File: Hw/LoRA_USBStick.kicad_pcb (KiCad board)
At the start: 2 copper layers, 65 x 18 mm, 16 parts, among them J10 USB_B, J4 SWD, SW1 RST, U1 ATSAMD21E, U2 RFM95W-868S2, U7 AP2114H-3.3TRG1

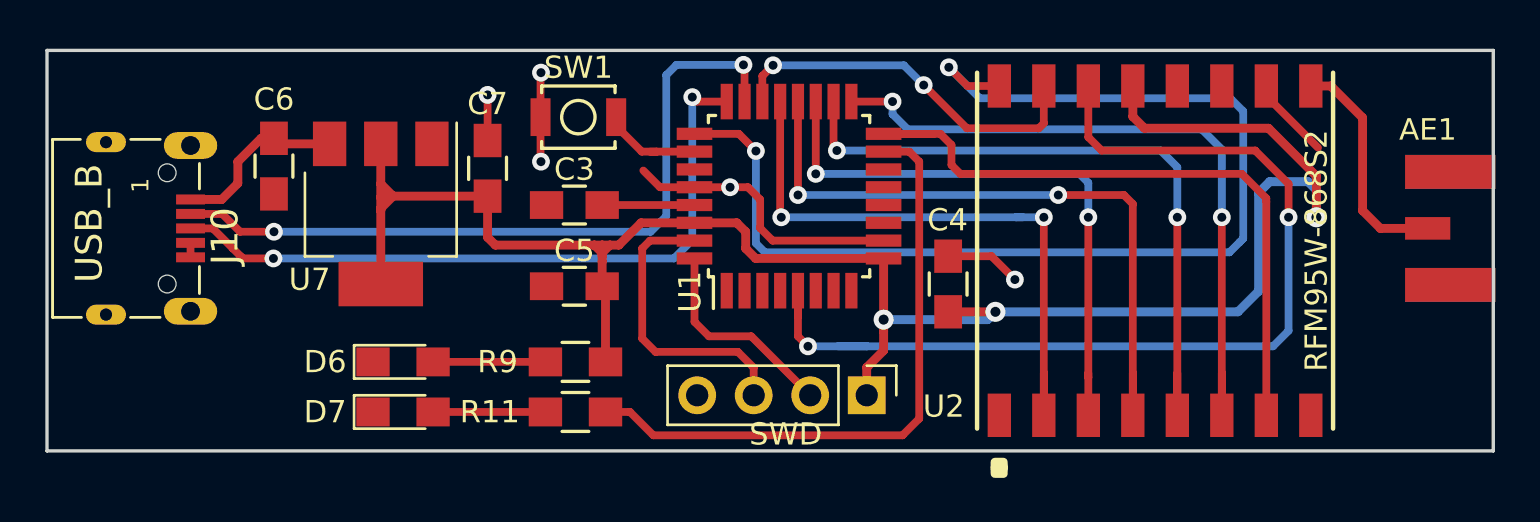
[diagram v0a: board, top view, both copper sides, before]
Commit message: Update kicad 5
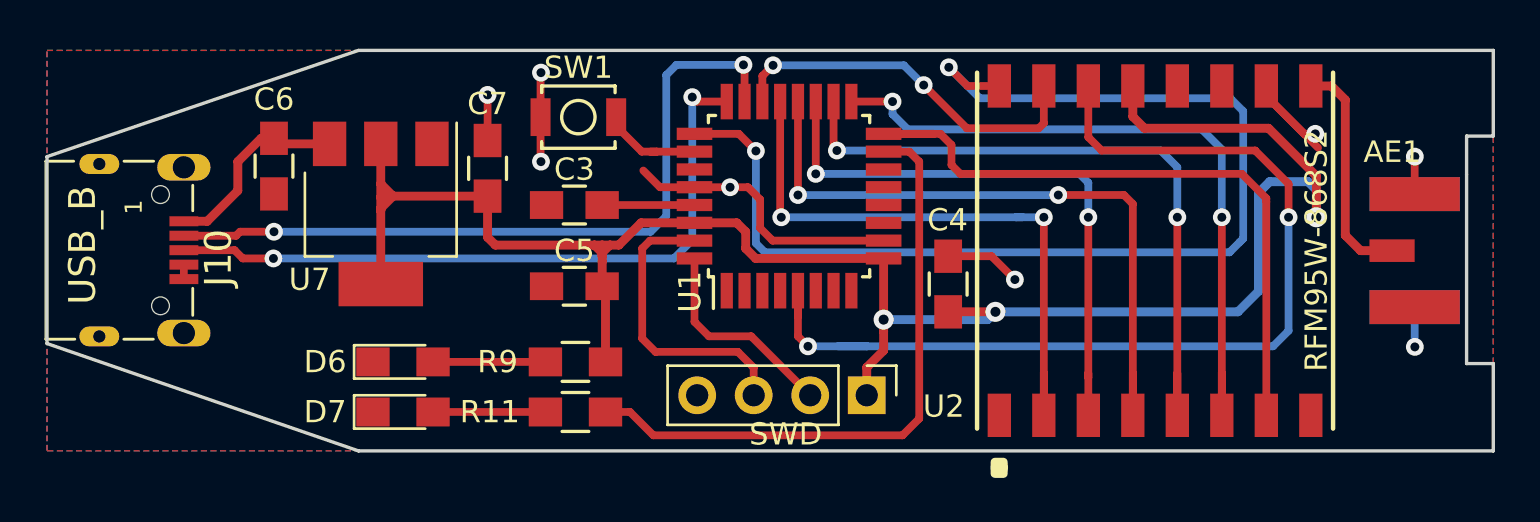
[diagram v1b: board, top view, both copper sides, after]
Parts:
- added G***: LOGO, Aesthetics:electronic_cats_logo_8x6, B.Cu at (196.8, 102.8)
- moved AE1 1.89 mm to (215.5, 104.0)
- moved J10 1.02 mm to (157.1, 104.0)
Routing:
- net GND: track 26.7 -> 33.1 mm, vias 5 -> 8
- net VBUS: track 8.06 -> 8.96 mm
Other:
- outline, holes or cut-outs redrawn
- board text added: "3.3v"
- board text added: "Compatible with LoRaWAN®"
- board text added: "GND"
- board text added: "Notas:"
- board text added: "SWCLK"
- board text added: "SWDIO"
- board text added: "USB-Stick V1.0 CatWAN"

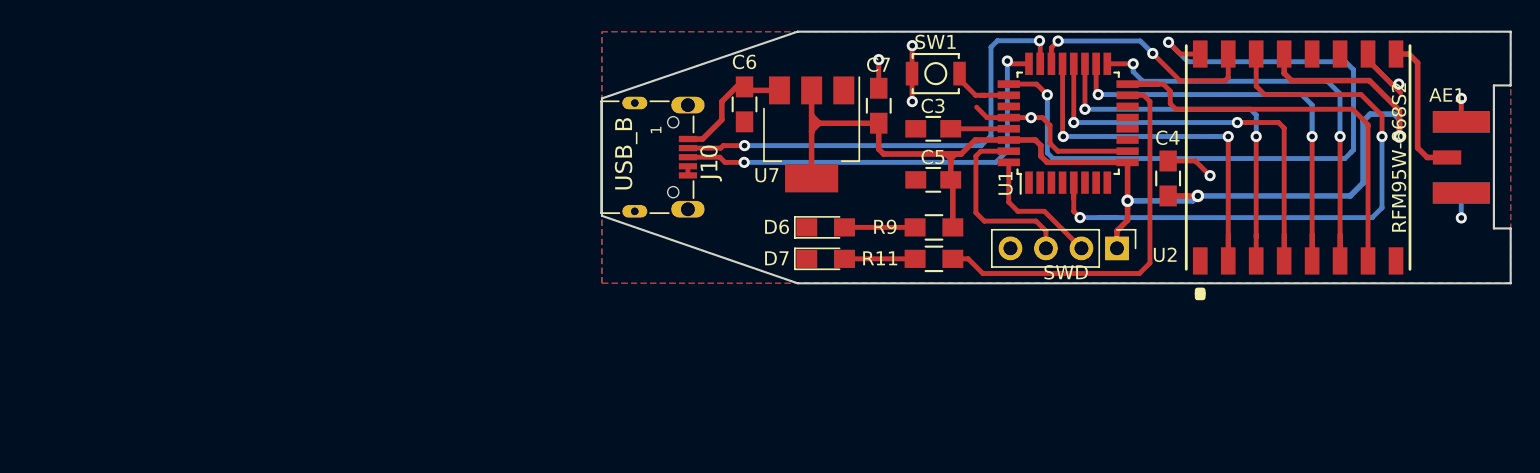
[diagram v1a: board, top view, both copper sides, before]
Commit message: Update measure for case
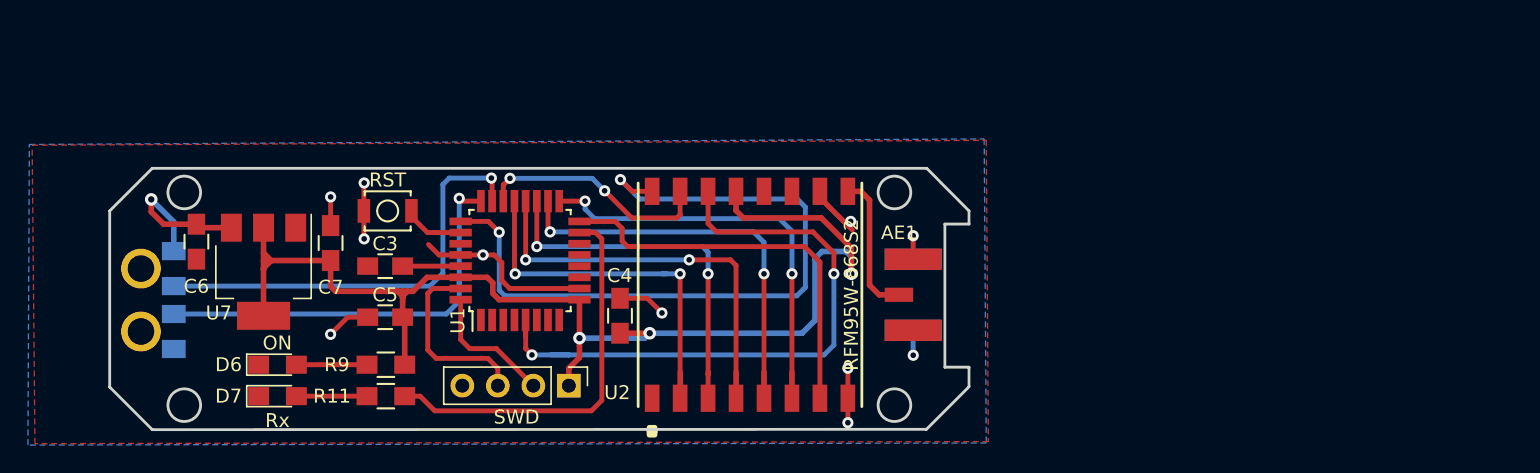
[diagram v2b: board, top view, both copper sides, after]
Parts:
- J10: footprint USB:629105150521 -> USB:629004113921; moved to B.Cu
- moved AE1 40.4 mm to (176.3, 113.8)
- moved C3 40.4 mm to (136.5, 111.8)
- moved C4 40.4 mm to (153.3, 115.3)
- moved C5 40.4 mm to (136.5, 115.4)
- moved C7 40.4 mm to (132.6, 110.1)
- moved D6 40.4 mm to (128.8, 118.8)
- moved D7 40.4 mm to (128.8, 121.1)
- moved J4 40.4 mm to (149.6, 120.3)
- moved R11 40.4 mm to (136.5, 121.1)
- moved R9 40.4 mm to (136.5, 118.8)
- moved SW1 40.4 mm to (136.7, 107.8)
- moved U1 40.4 mm to (146.1, 111.4)
- moved U2 40.4 mm to (162.6, 113.8)
- moved U7 40.4 mm to (127.8, 112.2)
- moved C6 40.4 mm to (123.0, 110.0)
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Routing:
- net GND: track 33.1 -> 39.5 mm, vias 8 -> 11
- net VBUS: track 8.96 -> 11.5 mm, vias 0 -> 1
- net /D-: track 33.7 -> 31.3 mm, vias 2 -> 1
- net /D+: track 31.4 -> 30.5 mm, vias 2 -> 1
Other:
- board size 65 x 18 mm -> 61.5 x 18.7 mm
- board text added: "ON"

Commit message: Fix notes text
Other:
- board text added: "Notes:"
- board text removed: "Notas:"
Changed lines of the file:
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@@
     (visible_elements FFFFFF7F)
     (pcbplotparams
-      (layerselection 0x010fc_80000001)
-      (usegerberextensions false)
+      (layerselection 0x010fc_ffffffff)
+      (usegerberextensions true)
       (usegerberattributes false)
       (usegerberadvancedattributes false)
@@
       (drillshape 0)
       (scaleselection 1)
-      (outputdirectory "/Volumes/Macintosh_HD/Documents/Electronic_Cats/Proyectos/Hw/agroin/Hw/Gerbers/"))
+      (outputdirectory "USB_stick_gerber/"))
   )
   (net 0 "")
@@
     (effects (font (size 1.5 1.5) (thickness 0.3)) (justify mirror))
   )
-  (gr_text Notas: (at 137.292 106.0724) (layer B.SilkS)
+  (gr_text Notes: (at 137.292 106.0724) (layer B.SilkS)
     (effects (font (size 1.5 1.5) (thickness 0.3)) (justify mirror))
   )

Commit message: Change USB side version 1.1v
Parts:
- C6, C7, U7: moved to B.Cu
- J10: moved to F.Cu
- moved C6 4.23 mm to (123.1, 114.2), turned to 90 degrees
- moved C7 4.13 mm to (132.5, 114.2), turned to 270 degrees
- moved SW1 2.58 mm to (136.7, 110.4)
- moved C3 1.44 mm to (136.7, 113.2)
- moved C5 0.16 mm to (136.7, 115.4)
- turned J10 to 270 degrees
- turned U7 to 90 degrees
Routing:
- net VBUS: track 11.5 -> 6.72 mm
- net +3V3: track 87.7 -> 92.1 mm, vias 3 -> 4
- net GND: track 39.5 -> 37.2 mm, vias 11 -> 12
- net /D+: track 30.5 -> 28.2 mm, vias 1 -> 0
- net /SWCLK: track 13.3 -> 11.6 mm
- net /D-: track 31.3 -> 31.9 mm, vias 1 -> 2
- net /RST: track 4.70 -> 4.18 mm
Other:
- board text added: "USB-Stick V1.1 CatWAN"
- board text removed: "USB-Stick V1.0 CatWAN"

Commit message: Fix vias on PCB
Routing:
- net GND: track 37.2 -> 41.1 mm, vias 12 -> 14
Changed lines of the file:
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@@
     (thickness 1.6)
     (drawings 37)
-    (tracks 255)
+    (tracks 261)
     (zones 0)
     (modules 17)
@@
   )
   (layers
-    (0 F.Cu signal hide)
-    (31 B.Cu signal hide)
+    (0 F.Cu signal)
+    (31 B.Cu signal)
     (32 B.Adhes user)
     (33 F.Adhes user)
@@
   (via (at 133.9 113.2) (size 0.8) (drill 0.4) (layers F.Cu B.Cu) (net 1))
   (segment (start 135.4 113.2) (end 133.9 113.2) (width 0.35) (layer F.Cu) (net 1))
+  (via (at 121.4 108.9) (size 0.8) (drill 0.4) (layers F.Cu B.Cu) (net 1))
+  (segment (start 121.3744 108.9256) (end 121.4 108.9) (width 0.35) (layer F.Cu) (net 1))
+  (segment (start 121.3744 110.6984) (end 121.3744 108.9256) (width 0.35) (layer F.Cu) (net 1))
+  (via (at 123.45 110.7) (size 0.8) (drill 0.4) (layers F.Cu B.Cu) (net 1))
+  (segment (start 123.4484 110.6984) (end 123.45 110.7) (width 0.35) (layer F.Cu) (net 1))
+  (segment (start 121.3744 110.6984) (end 123.4484 110.6984) (width 0.35) (layer F.Cu) (net 1))
   (segment (start 170.517 106.4224) (end 169.592 106.4224) (width 0.4) (layer F.Cu) (net 2))
   (segment (start 171.142 107.0474) (end 170.517 106.4224) (width 0.4) (layer F.Cu) (net 2))

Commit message: Add v2.0
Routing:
- net /DIO2: track 52.5 -> 17.2 mm
- net /DIO0: track 45.8 -> 34.8 mm, vias 2 -> 4
- net /Rx_LED: track 28.2 -> 34.6 mm, vias 0 -> 2
- net GND: track 41.1 -> 46.7 mm, vias 14 -> 18
- net +3V3: track 92.1 -> 88.8 mm, vias 4 -> 3
- net /DIO5: track 30.9 -> 28.6 mm, vias 0 -> 2
- net /MISO: track 28.1 -> 25.8 mm
- net /SS: track 30.9 -> 28.7 mm
- net /MOSI: track 26.3 -> 28.2 mm
- net /SCK: track 30.8 -> 30.3 mm
- net /DIO1: track 16.9 -> 17.1 mm, vias 2 -> 0
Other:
- net class Default: clearance 0.2 -> 0.3
- rule trace_clearance: 0.2 -> 0.3

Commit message: Update V2.0
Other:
- board text added: "USB-Stick V2.0 CatWAN"
- board text removed: "USB-Stick V1.1 CatWAN"
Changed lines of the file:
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@@
   )
   (layers
-    (0 F.Cu signal)
-    (31 B.Cu signal)
+    (0 F.Cu signal hide)
+    (31 B.Cu signal hide)
     (32 B.Adhes user)
     (33 F.Adhes user)
@@
   (gr_line (start 116.7892 107.823) (end 116.7892 120.4214) (layer Edge.Cuts) (width 0.2))
   (gr_line (start 119.8372 104.775) (end 175.2346 104.775) (layer Edge.Cuts) (width 0.2))
-  (gr_text "USB-Stick V1.1\nCatWAN" (at 162.142 107.5224) (layer B.SilkS)
+  (gr_text "USB-Stick V2.0\nCatWAN" (at 162.142 107.5224) (layer B.SilkS)
     (effects (font (size 1.5 1.5) (thickness 0.3)) (justify mirror))
   )

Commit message: Update V3.0
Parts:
- SW1: footprint Buttons_Switches_SMD:SW_SPST_B3U-1000P -> Button_Switch_SMD:SW_SPST_TL3342
- moved D6 12.3 mm to (128.0, 106.5)
- moved R9 12.3 mm to (136.0, 106.5)
- moved SW1 8.52 mm to (129.1, 114.2), turned to 270 degrees
- moved D7 0.99 mm to (128.0, 121.7)
- moved R11 0.80 mm to (136.0, 121.7)
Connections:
- net /DI1 renamed Net-(U1-Pad3)
- net /DI2 renamed Net-(U1-Pad2)
- net /DI3 renamed Net-(U1-Pad1)
- net /DO1 renamed Net-(U1-Pad8)
- net /DO2 renamed Net-(U1-Pad7)
- net /DO3 renamed Net-(U1-Pad6)
- net /Rx renamed Net-(U1-Pad14)
- net /Tx renamed Net-(U1-Pad13)
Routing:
- net /RST: track 4.18 -> 17.9 mm
- net GND: track 46.7 -> 42.0 mm, vias 18 -> 16
- net Net-(D7-Pad2): track 5.05 -> 6.90 mm
- net /Rx_LED: track 34.6 -> 36.4 mm
- net /D+: track 28.2 -> 27.1 mm
- net +3V3: track 88.8 -> 88.7 mm, vias 3 -> 2
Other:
- board text removed: "Notes:"
